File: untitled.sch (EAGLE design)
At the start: 31 parts, among them IC1 STM8S003F3

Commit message: second commit
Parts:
- added TP15: TPB2,54, testpad:TPB2,54
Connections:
- removed net N$25: C1.2, C5.2, IC1.GND, SWIM.3
- new net N$1: IC1.PC4/TIM1_CH4/CLK_CCO/AIN2/[!TIM1_CH2!], TP15.TP
- net GND: now also C1.2, C5.2, IC1.GND, SWIM.3
- net NEXT: now also IC1.PC7/SPI_MISO/[TIM1_CH2]; no longer IC1.PD4/UART1_CK/TIM2_CH1/BEEP
- net PLAY_PAUSE: now also IC1.PD3/AIN4/TIM2_CH2/ADC_ETR; no longer IC1.PD6/UART1_RX/AIN6
- net PRE: now also IC1.PD2/AIN3/[TIM2_CH3]; no longer IC1.PD5/UART1_TX/AIN5
- net VOL+: now also IC1.PC5/SPI_SCK/[TIM2_CH1]; no longer IC1.PD2/AIN3/[TIM2_CH3]
- net VOL-: now also IC1.PC6/SPI_MOSI/[TIM1_CH1]; no longer IC1.PD3/AIN4/TIM2_CH2/ADC_ETR

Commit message: third commit
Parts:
- removed TP1, TP2: TPB2,54, testpad:TPB2,54
- added SWIM1: (no value), con-lstb:MA04-1
- added U$2: MCP1825SOT-223-3, SteelCaveRobotics-Power:MCP1825SOT-223-3
- LED1, LED2, LED3: device led:LEDCHIP-LED0805 -> led:LEDCHIPLED_0603
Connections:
- removed net N$13: TP1.TP, U$1.UART_TX/PIO1
- removed net N$14: TP2.TP, U$1.UART_RX/PIO0
- new net VDD: TP13.TP, U$2.IN
- net GND: now also U$2.GND@2
- net LED0: now also LED3.C; no longer LED1.C
- net LED2: now also LED1.C; no longer LED3.C
- net N$1: now also IC1.PD6/UART1_RX/AIN6; no longer IC1.PC4/TIM1_CH4/CLK_CCO/AIN2/[!TIM1_CH2!]
- net N$20: now also SWIM1.1
- net N$21: now also SWIM1.2
- net N$22: now also SWIM1.3
- net N$23: now also SWIM1.4
- net N$4: now also LED1.A; no longer LED3.A
- net N$6: now also LED3.A; no longer LED1.A
- net VCC: now also U$2.+3V3; no longer TP13.TP
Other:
- moved on the sheet: LED1, LED3, TP13, TP15

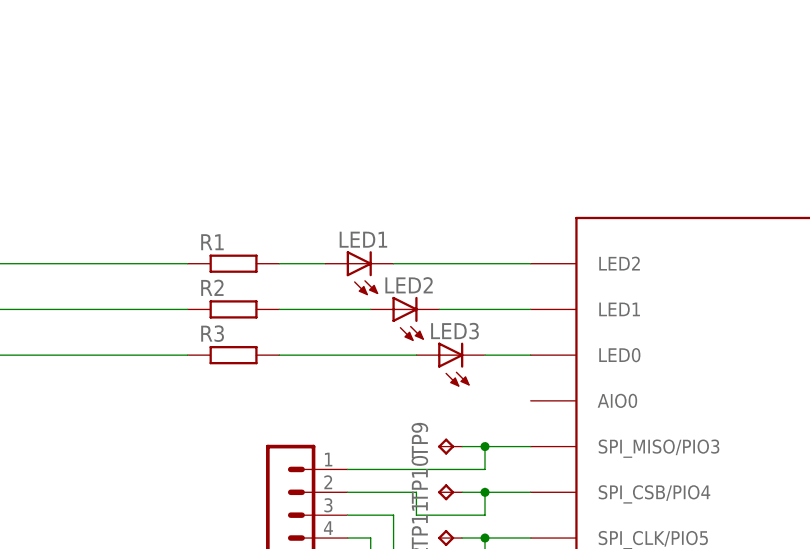
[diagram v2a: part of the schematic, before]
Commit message: removed leds
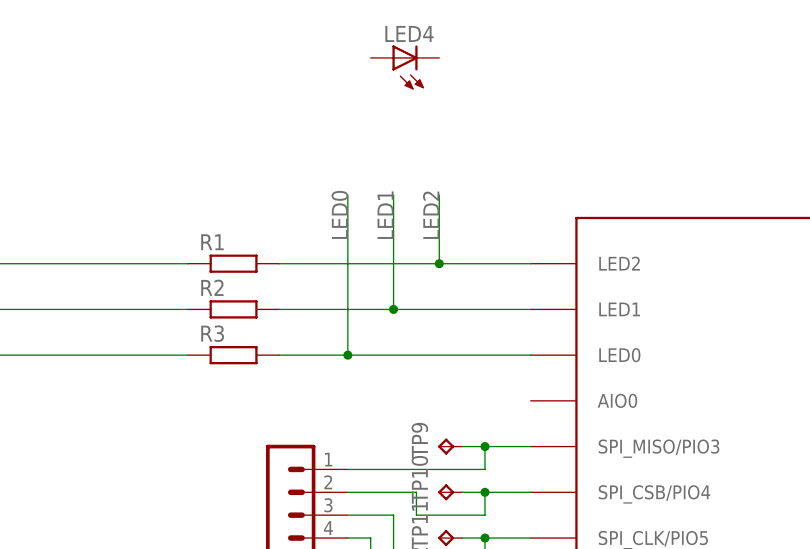
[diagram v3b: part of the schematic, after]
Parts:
- removed LED1, LED2, LED3: (no value), led:LEDCHIPLED_0603
- added LED4: (no value), led:LEDCHIPLED_0603
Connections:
- removed net N$4: LED1.A, R1.2
- removed net N$5: LED2.A, R2.2
- removed net N$6: LED3.A, R3.2
- net LED0: now also R3.2; no longer LED3.C
- net LED1: now also R2.2; no longer LED2.C
- net LED2: now also R1.2; no longer LED1.C
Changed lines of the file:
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@@
 <?xml version="1.0" encoding="utf-8"?>
 <!DOCTYPE eagle SYSTEM "eagle.dtd">
-<eagle version="7.3.0">
+<eagle version="7.4.0">
 <drawing>
 <settings>
@@
 <part name="TP15" library="testpad" deviceset="TP" device="B2,54"/>
 <part name="SWIM1" library="con-lstb" deviceset="MA04-1" device=""/>
-<part name="LED1" library="led" deviceset="LED" device="CHIPLED_0603"/>
-<part name="LED2" library="led" deviceset="LED" device="CHIPLED_0603"/>
-<part name="LED3" library="led" deviceset="LED" device="CHIPLED_0603"/>
 <part name="P+5" library="supply1" deviceset="VCC" device=""/>
 <part name="VDD1" library="supply1" deviceset="VDD" device=""/>
 <part name="U$2" library="SteelCaveRobotics-Power" deviceset="MCP1825" device="SOT-223-3"/>
 <part name="GND5" library="supply1" deviceset="GND" device=""/>
+<part name="LED4" library="led" deviceset="LED" device="CHIPLED_0603"/>
 </parts>
 <sheets>
@@
 <instance part="TP15" gate="G$1" x="238.76" y="-5.08" rot="R270"/>
 <instance part="SWIM1" gate="1" x="-63.5" y="12.7" rot="MR180"/>
-<instance part="LED1" gate="G$1" x="-55.88" y="40.64" rot="R90"/>
-<instance part="LED2" gate="G$1" x="-50.8" y="35.56" rot="R90"/>
-<instance part="LED3" gate="G$1" x="-45.72" y="30.48" rot="R90"/>
 <instance part="P+5" gate="VCC" x="-91.44" y="-33.02" rot="R270"/>
 <instance part="VDD1" gate="G$1" x="-127" y="-33.02" rot="R90"/>
 <instance part="U$2" gate="G$1" x="-109.22" y="-35.56"/>
 <instance part="GND5" gate="1" x="-109.22" y="-50.8"/>
+<instance part="LED4" gate="G$1" x="-50.8" y="63.5" rot="R90"/>
 </instances>
 <busses>
 </busses>
 <nets>
-<net name="N$4" class="0">
-<segment>
-<pinref part="R1" gate="G$1" pin="2"/>
-<wire x1="-58.42" y1="40.64" x2="-63.5" y2="40.64" width="0.1524" layer="91"/>
-<pinref part="LED1" gate="G$1" pin="A"/>
-</segment>
-</net>
-<net name="N$5" class="0">
-<segment>
-<pinref part="R2" gate="G$1" pin="2"/>
-<wire x1="-53.34" y1="35.56" x2="-63.5" y2="35.56" width="0.1524" layer="91"/>
-<pinref part="LED2" gate="G$1" pin="A"/>
-</segment>
-</net>
-<net name="N$6" class="0">
-<segment>
-<pinref part="R3" gate="G$1" pin="2"/>
-<wire x1="-48.26" y1="30.48" x2="-63.5" y2="30.48" width="0.1524" layer="91"/>
-<pinref part="LED3" gate="G$1" pin="A"/>
-</segment>
-</net>
 <net name="VCC" class="0">
 <segment>
@@
 <segment>
 <pinref part="U$1" gate="G$1" pin="LED2"/>
-<wire x1="-35.56" y1="40.64" x2="-50.8" y2="40.64" width="0.1524" layer="91"/>
-<pinref part="LED1" gate="G$1" pin="C"/>
+<wire x1="-35.56" y1="40.64" x2="-45.72" y2="40.64" width="0.1524" layer="91"/>
+<pinref part="R1" gate="G$1" pin="2"/>
+<wire x1="-45.72" y1="40.64" x2="-63.5" y2="40.64" width="0.1524" layer="91"/>
+<wire x1="-45.72" y1="40.64" x2="-45.72" y2="48.26" width="0.1524" layer="91"/>
+<junction x="-45.72" y="40.64"/>
+<label x="-45.72" y="43.18" size="1.778" layer="95" rot="R90"/>
 </segment>
 </net>
@@
 <segment>
 <pinref part="U$1" gate="G$1" pin="LED1"/>
-<wire x1="-35.56" y1="35.56" x2="-45.72" y2="35.56" width="0.1524" layer="91"/>
-<pinref part="LED2" gate="G$1" pin="C"/>
+<wire x1="-35.56" y1="35.56" x2="-50.8" y2="35.56" width="0.1524" layer="91"/>
+<pinref part="R2" gate="G$1" pin="2"/>
+<wire x1="-50.8" y1="35.56" x2="-63.5" y2="35.56" width="0.1524" layer="91"/>
+<wire x1="-50.8" y1="35.56" x2="-50.8" y2="48.26" width="0.1524" layer="91"/>
+<junction x="-50.8" y="35.56"/>
+<label x="-50.8" y="43.18" size="1.778" layer="95" rot="R90"/>
 </segment>
 </net>
@@
 <segment>
 <pinref part="U$1" gate="G$1" pin="LED0"/>
-<wire x1="-35.56" y1="30.48" x2="-40.64" y2="30.48" width="0.1524" layer="91"/>
-<pinref part="LED3" gate="G$1" pin="C"/>
-</segment>
-</net>
+<pinref part="R3" gate="G$1" pin="2"/>
+<wire x1="-35.56" y1="30.48" x2="-55.88" y2="30.48" width="0.1524" layer="91"/>
+<wire x1="-55.88" y1="30.48" x2="-63.5" y2="30.48" width="0.1524" layer="91"/>
+<wire x1="-55.88" y1="30.48" x2="-55.88" y2="48.26" width="0.1524" layer="91"/>
+<junction x="-55.88" y="30.48"/>
+<label x="-55.88" y="43.18" size="1.778" layer="95" rot="R90"/>
+</segment>
+</net>

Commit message: added tx signal + led
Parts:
- added R6: 100, rcl:R-EU_R0805
- added TP1: TPB2,54, testpad:TPB2,54
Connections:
- new net N$29: LED4.C, R6.1
- new net N$5: IC1.PD5/UART1_TX/AIN5, TP1.TP
- new net N$6: IC1.PB5/I2C_SDA/[TIM1_BKIN], LED4.A
- net GND: now also R6.2
- net LED0: now also IC1.PA3/TIM2_CH3/[SPI_NSS]; no longer IC1.PB5/I2C_SDA/[TIM1_BKIN]
- net LED1: no longer IC1.PB4/I2C_SCL/[ADC_ETR]
- net LED2: no longer IC1.PA3/TIM2_CH3/[SPI_NSS]
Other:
- moved on the sheet: LED4
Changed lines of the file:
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@@
 <?xml version="1.0" encoding="utf-8"?>
 <!DOCTYPE eagle SYSTEM "eagle.dtd">
-<eagle version="7.4.0">
+<eagle version="7.3.0">
 <drawing>
 <settings>
@@
 <part name="GND5" library="supply1" deviceset="GND" device=""/>
 <part name="LED4" library="led" deviceset="LED" device="CHIPLED_0603"/>
+<part name="TP1" library="testpad" deviceset="TP" device="B2,54"/>
+<part name="R6" library="rcl" deviceset="R-EU_" device="R0805" value="100"/>
+<part name="GND4" library="supply1" deviceset="GND" device=""/>
 </parts>
 <sheets>
@@
 <instance part="U$2" gate="G$1" x="-109.22" y="-35.56"/>
 <instance part="GND5" gate="1" x="-109.22" y="-50.8"/>
-<instance part="LED4" gate="G$1" x="-50.8" y="63.5" rot="R90"/>
+<instance part="LED4" gate="G$1" x="236.22" y="27.94" rot="R90"/>
+<instance part="TP1" gate="G$1" x="238.76" y="-2.54" rot="R270"/>
+<instance part="R6" gate="G$1" x="248.92" y="27.94"/>
+<instance part="GND4" gate="1" x="259.08" y="27.94" rot="R90"/>
 </instances>
 <busses>
@@
 <wire x1="-109.22" y1="-43.18" x2="-109.22" y2="-48.26" width="0.1524" layer="91"/>
 </segment>
+<segment>
+<pinref part="R6" gate="G$1" pin="2"/>
+<pinref part="GND4" gate="1" pin="GND"/>
+<wire x1="254" y1="27.94" x2="256.54" y2="27.94" width="0.1524" layer="91"/>
+</segment>
 </net>
 <net name="N$9" class="0">
@@
 <net name="LED2" class="0">
 <segment>
-<pinref part="IC1" gate="G$1" pin="PA3/TIM2_CH3/[SPI_NSS]"/>
-<wire x1="223.52" y1="33.02" x2="238.76" y2="33.02" width="0.1524" layer="91"/>
-<label x="233.68" y="33.02" size="1.778" layer="95"/>
-</segment>
-<segment>
 <pinref part="U$1" gate="G$1" pin="LED2"/>
 <wire x1="-35.56" y1="40.64" x2="-45.72" y2="40.64" width="0.1524" layer="91"/>
@@
 <net name="LED1" class="0">
 <segment>
-<pinref part="IC1" gate="G$1" pin="PB4/I2C_SCL/[ADC_ETR]"/>
-<wire x1="223.52" y1="30.48" x2="238.76" y2="30.48" width="0.1524" layer="91"/>
-<label x="233.68" y="30.48" size="1.778" layer="95"/>
-</segment>
-<segment>
 <pinref part="U$1" gate="G$1" pin="LED1"/>
 <wire x1="-35.56" y1="35.56" x2="-50.8" y2="35.56" width="0.1524" layer="91"/>
@@
 <net name="LED0" class="0">
 <segment>
-<pinref part="IC1" gate="G$1" pin="PB5/I2C_SDA/[TIM1_BKIN]"/>
-<wire x1="223.52" y1="27.94" x2="238.76" y2="27.94" width="0.1524" layer="91"/>
-<label x="233.68" y="27.94" size="1.778" layer="95"/>
-</segment>
-<segment>
 <pinref part="U$1" gate="G$1" pin="LED0"/>
 <pinref part="R3" gate="G$1" pin="2"/>
@@
 <label x="-55.88" y="43.18" size="1.778" layer="95" rot="R90"/>
 </segment>
+<segment>
+<pinref part="IC1" gate="G$1" pin="PA3/TIM2_CH3/[SPI_NSS]"/>
+<wire x1="223.52" y1="33.02" x2="238.76" y2="33.02" width="0.1524" layer="91"/>
+<label x="233.68" y="33.02" size="1.778" layer="95"/>
+</segment>
 </net>
 <net name="N$1" class="0">
@@
 </segment>
 </net>
+<net name="N$5" class="0">
+<segment>
+<pinref part="IC1" gate="G$1" pin="PD5/UART1_TX/AIN5"/>
+<pinref part="TP1" gate="G$1" pin="TP"/>
+<wire x1="223.52" y1="-2.54" x2="236.22" y2="-2.54" width="0.1524" layer="91"/>
+</segment>
+</net>
+<net name="N$6" class="0">
+<segment>
+<pinref part="IC1" gate="G$1" pin="PB5/I2C_SDA/[TIM1_BKIN]"/>
+<pinref part="LED4" gate="G$1" pin="A"/>
+<wire x1="223.52" y1="27.94" x2="233.68" y2="27.94" width="0.1524" layer="91"/>
+</segment>
+</net>
+<net name="N$29" class="0">
+<segment>
+<pinref part="LED4" gate="G$1" pin="C"/>
+<pinref part="R6" gate="G$1" pin="1"/>
+<wire x1="241.3" y1="27.94" x2="243.84" y2="27.94" width="0.1524" layer="91"/>
+</segment>
+</net>

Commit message: new design
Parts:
- removed TP10, TP11, TP12, TP9: TPB2,54, testpad:TPB2,54
- added C6, C7: 104, rcl:C-EUC0805
- added LED1: (no value), led:LEDCHIPLED_0603
- added R10, R7, R8, R9: (no value), rcl:R-EU_R0805
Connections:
- new net N$30: R8.2, U$1.SPI_CSB/PIO4
- new net N$31: R9.1, SWIM1.3
- new net N$32: R10.2, U$1.SPI_MOSI/PIO2
- new net N$33: R10.1, SWIM1.4
- new net N$34: LED1.C, U$1.LED1
- net GND: now also C6.2, C7.2
- net LED1: now also LED1.A; no longer U$1.LED1
- net N$20: now also R7.2; no longer SWIM1.1, TP9.TP
- net N$21: now also R7.1, SWIM1.1; no longer SWIM1.2, TP10.TP, U$1.SPI_CSB/PIO4
- net N$22: now also R9.2; no longer SWIM1.3, TP11.TP
- net N$23: now also R8.1, SWIM1.2; no longer SWIM1.4, TP12.TP, U$1.SPI_MOSI/PIO2
- net VCC: now also C7.1
- net VDD: now also C6.1
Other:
- moved on the sheet: SWIM1
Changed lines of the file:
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@@
 <part name="TP7" library="testpad" deviceset="TP" device="B2,54"/>
 <part name="TP8" library="testpad" deviceset="TP" device="B2,54"/>
-<part name="TP9" library="testpad" deviceset="TP" device="B2,54"/>
-<part name="TP10" library="testpad" deviceset="TP" device="B2,54"/>
-<part name="TP11" library="testpad" deviceset="TP" device="B2,54"/>
-<part name="TP12" library="testpad" deviceset="TP" device="B2,54"/>
 <part name="TP13" library="testpad" deviceset="TP" device="B2,54"/>
 <part name="TP14" library="testpad" deviceset="TP" device="B2,54"/>
@@
 <part name="R6" library="rcl" deviceset="R-EU_" device="R0805" value="100"/>
 <part name="GND4" library="supply1" deviceset="GND" device=""/>
+<part name="R7" library="rcl" deviceset="R-EU_" device="R0805"/>
+<part name="R8" library="rcl" deviceset="R-EU_" device="R0805"/>
+<part name="R9" library="rcl" deviceset="R-EU_" device="R0805"/>
+<part name="R10" library="rcl" deviceset="R-EU_" device="R0805"/>
+<part name="C6" library="rcl" deviceset="C-EU" device="C0805" value="104"/>
+<part name="C7" library="rcl" deviceset="C-EU" device="C0805" value="104"/>
+<part name="LED1" library="led" deviceset="LED" device="CHIPLED_0603"/>
 </parts>
 <sheets>
@@
 <instance part="TP7" gate="G$1" x="45.72" y="25.4" rot="R270"/>
 <instance part="TP8" gate="G$1" x="45.72" y="20.32" rot="R270"/>
-<instance part="TP9" gate="G$1" x="-45.72" y="20.32" rot="R90"/>
-<instance part="TP10" gate="G$1" x="-45.72" y="15.24" rot="R90"/>
-<instance part="TP11" gate="G$1" x="-45.72" y="10.16" rot="R90"/>
-<instance part="TP12" gate="G$1" x="-45.72" y="5.08" rot="R90"/>
 <instance part="TP13" gate="G$1" x="-121.92" y="-25.4"/>
 <instance part="TP14" gate="G$1" x="-53.34" y="-40.64" rot="R90"/>
@@
 <instance part="GND3" gate="1" x="129.54" y="5.08"/>
 <instance part="TP15" gate="G$1" x="238.76" y="-5.08" rot="R270"/>
-<instance part="SWIM1" gate="1" x="-63.5" y="12.7" rot="MR180"/>
+<instance part="SWIM1" gate="1" x="-66.04" y="12.7" rot="MR180"/>
 <instance part="P+5" gate="VCC" x="-91.44" y="-33.02" rot="R270"/>
 <instance part="VDD1" gate="G$1" x="-127" y="-33.02" rot="R90"/>
 <instance part="U$2" gate="G$1" x="-109.22" y="-35.56"/>
-<instance part="GND5" gate="1" x="-109.22" y="-50.8"/>
+<instance part="GND5" gate="1" x="-109.22" y="-55.88"/>
 <instance part="LED4" gate="G$1" x="236.22" y="27.94" rot="R90"/>
 <instance part="TP1" gate="G$1" x="238.76" y="-2.54" rot="R270"/>
 <instance part="R6" gate="G$1" x="248.92" y="27.94"/>
 <instance part="GND4" gate="1" x="259.08" y="27.94" rot="R90"/>
+<instance part="R7" gate="G$1" x="-45.72" y="20.32"/>
+<instance part="R8" gate="G$1" x="-45.72" y="15.24"/>
+<instance part="R9" gate="G$1" x="-45.72" y="10.16"/>
+<instance part="R10" gate="G$1" x="-45.72" y="5.08"/>
+<instance part="C6" gate="G$1" x="-121.92" y="-40.64"/>
+<instance part="C7" gate="G$1" x="-96.52" y="-40.64"/>
+<instance part="LED1" gate="G$1" x="-45.72" y="35.56" rot="R90"/>
 </instances>
 <busses>
@@
 <pinref part="U$2" gate="G$1" pin="+3V3"/>
 <pinref part="P+5" gate="VCC" pin="VCC"/>
-<wire x1="-99.06" y1="-33.02" x2="-93.98" y2="-33.02" width="0.1524" layer="91"/>
+<wire x1="-99.06" y1="-33.02" x2="-96.52" y2="-33.02" width="0.1524" layer="91"/>
+<pinref part="C7" gate="G$1" pin="1"/>
+<wire x1="-96.52" y1="-33.02" x2="-93.98" y2="-33.02" width="0.1524" layer="91"/>
+<wire x1="-96.52" y1="-38.1" x2="-96.52" y2="-33.02" width="0.1524" layer="91"/>
+<junction x="-96.52" y="-33.02"/>
 </segment>
 </net>
@@
 <pinref part="GND5" gate="1" pin="GND"/>
 <wire x1="-109.22" y1="-43.18" x2="-109.22" y2="-48.26" width="0.1524" layer="91"/>
+<pinref part="C6" gate="G$1" pin="2"/>
+<wire x1="-109.22" y1="-48.26" x2="-109.22" y2="-53.34" width="0.1524" layer="91"/>
+<wire x1="-121.92" y1="-45.72" x2="-121.92" y2="-48.26" width="0.1524" layer="91"/>
+<wire x1="-121.92" y1="-48.26" x2="-109.22" y2="-48.26" width="0.1524" layer="91"/>
+<junction x="-109.22" y="-48.26"/>
+<pinref part="C7" gate="G$1" pin="2"/>
+<wire x1="-96.52" y1="-45.72" x2="-96.52" y2="-48.26" width="0.1524" layer="91"/>
+<wire x1="-96.52" y1="-48.26" x2="-109.22" y2="-48.26" width="0.1524" layer="91"/>
 </segment>
 <segment>
@@
 <segment>
 <pinref part="U$1" gate="G$1" pin="SPI_MISO/PIO3"/>
-<pinref part="TP9" gate="G$1" pin="TP"/>
 <wire x1="-35.56" y1="20.32" x2="-40.64" y2="20.32" width="0.1524" layer="91"/>
-<pinref part="SWIM1" gate="1" pin="1"/>
-<wire x1="-40.64" y1="20.32" x2="-43.18" y2="20.32" width="0.1524" layer="91"/>
-<wire x1="-55.88" y1="17.78" x2="-40.64" y2="17.78" width="0.1524" layer="91"/>
-<wire x1="-40.64" y1="17.78" x2="-40.64" y2="20.32" width="0.1524" layer="91"/>
-<junction x="-40.64" y="20.32"/>
-</segment>
-</net>
-<net name="N$21" class="0">
-<segment>
-<pinref part="U$1" gate="G$1" pin="SPI_CSB/PIO4"/>
-<pinref part="TP10" gate="G$1" pin="TP"/>
-<wire x1="-35.56" y1="15.24" x2="-40.64" y2="15.24" width="0.1524" layer="91"/>
-<pinref part="SWIM1" gate="1" pin="2"/>
-<wire x1="-40.64" y1="15.24" x2="-43.18" y2="15.24" width="0.1524" layer="91"/>
-<wire x1="-55.88" y1="15.24" x2="-48.26" y2="15.24" width="0.1524" layer="91"/>
-<wire x1="-48.26" y1="15.24" x2="-48.26" y2="12.7" width="0.1524" layer="91"/>
-<wire x1="-48.26" y1="12.7" x2="-40.64" y2="12.7" width="0.1524" layer="91"/>
-<wire x1="-40.64" y1="12.7" x2="-40.64" y2="15.24" width="0.1524" layer="91"/>
-<junction x="-40.64" y="15.24"/>
+<pinref part="R7" gate="G$1" pin="2"/>
 </segment>
 </net>
@@
 <segment>
 <pinref part="U$1" gate="G$1" pin="SPI_CLK/PIO5"/>
-<pinref part="TP11" gate="G$1" pin="TP"/>
 <wire x1="-35.56" y1="10.16" x2="-40.64" y2="10.16" width="0.1524" layer="91"/>
-<pinref part="SWIM1" gate="1" pin="3"/>
-<wire x1="-40.64" y1="10.16" x2="-43.18" y2="10.16" width="0.1524" layer="91"/>
-<wire x1="-55.88" y1="12.7" x2="-50.8" y2="12.7" width="0.1524" layer="91"/>
-<wire x1="-50.8" y1="12.7" x2="-50.8" y2="7.62" width="0.1524" layer="91"/>
-<wire x1="-50.8" y1="7.62" x2="-40.64" y2="7.62" width="0.1524" layer="91"/>
-<wire x1="-40.64" y1="7.62" x2="-40.64" y2="10.16" width="0.1524" layer="91"/>
-<junction x="-40.64" y="10.16"/>
-</segment>
-</net>
-<net name="N$23" class="0">
-<segment>
-<pinref part="U$1" gate="G$1" pin="SPI_MOSI/PIO2"/>
-<pinref part="TP12" gate="G$1" pin="TP"/>
-<wire x1="-35.56" y1="5.08" x2="-40.64" y2="5.08" width="0.1524" layer="91"/>
-<pinref part="SWIM1" gate="1" pin="4"/>
-<wire x1="-40.64" y1="5.08" x2="-43.18" y2="5.08" width="0.1524" layer="91"/>
-<wire x1="-55.88" y1="10.16" x2="-53.34" y2="10.16" width="0.1524" layer="91"/>
-<wire x1="-53.34" y1="10.16" x2="-53.34" y2="2.54" width="0.1524" layer="91"/>
-<wire x1="-53.34" y1="2.54" x2="-40.64" y2="2.54" width="0.1524" layer="91"/>
-<wire x1="-40.64" y1="2.54" x2="-40.64" y2="5.08" width="0.1524" layer="91"/>
-<junction x="-40.64" y="5.08"/>
+<pinref part="R9" gate="G$1" pin="2"/>
 </segment>
 </net>
@@
 <net name="LED1" class="0">
 <segment>
-<pinref part="U$1" gate="G$1" pin="LED1"/>
-<wire x1="-35.56" y1="35.56" x2="-50.8" y2="35.56" width="0.1524" layer="91"/>
 <pinref part="R2" gate="G$1" pin="2"/>
 <wire x1="-50.8" y1="35.56" x2="-63.5" y2="35.56" width="0.1524" layer="91"/>
 <wire x1="-50.8" y1="35.56" x2="-50.8" y2="48.26" width="0.1524" layer="91"/>
+<label x="-50.8" y="43.18" size="1.778" layer="95" rot="R90"/>
+<pinref part="LED1" gate="G$1" pin="A"/>
+<wire x1="-48.26" y1="35.56" x2="-50.8" y2="35.56" width="0.1524" layer="91"/>
 <junction x="-50.8" y="35.56"/>
-<label x="-50.8" y="43.18" size="1.778" layer="95" rot="R90"/>
 </segment>
 </net>
@@
 <wire x1="-121.92" y1="-27.94" x2="-121.92" y2="-33.02" width="0.1524" layer="91"/>
 <junction x="-121.92" y="-33.02"/>
+<pinref part="C6" gate="G$1" pin="1"/>
+<wire x1="-121.92" y1="-38.1" x2="-121.92" y2="-33.02" width="0.1524" layer="91"/>
 </segment>
 </net>
@@
 </segment>
 </net>
+<net name="N$30" class="0">
+<segment>
+<pinref part="U$1" gate="G$1" pin="SPI_CSB/PIO4"/>
+<wire x1="-35.56" y1="15.24" x2="-40.64" y2="15.24" width="0.1524" layer="91"/>
+<pinref part="R8" gate="G$1" pin="2"/>
+</segment>
+</net>
+<net name="N$32" class="0">
+<segment>
+<pinref part="U$1" gate="G$1" pin="SPI_MOSI/PIO2"/>
+<wire x1="-35.56" y1="5.08" x2="-40.64" y2="5.08" width="0.1524" layer="91"/>
+<pinref part="R10" gate="G$1" pin="2"/>
+</segment>
+</net>
+<net name="N$21" class="0">
+<segment>
+<pinref part="SWIM1" gate="1" pin="1"/>
+<wire x1="-58.42" y1="17.78" x2="-53.34" y2="17.78" width="0.1524" layer="91"/>
+<wire x1="-53.34" y1="17.78" x2="-53.34" y2="20.32" width="0.1524" layer="91"/>
+<pinref part="R7" gate="G$1" pin="1"/>
+<wire x1="-53.34" y1="20.32" x2="-50.8" y2="20.32" width="0.1524" layer="91"/>
+</segment>
+</net>
+<net name="N$23" class="0">
+<segment>
+<pinref part="R8" gate="G$1" pin="1"/>
+<pinref part="SWIM1" gate="1" pin="2"/>
+<wire x1="-50.8" y1="15.24" x2="-58.42" y2="15.24" width="0.1524" layer="91"/>
+</segment>
+</net>
+<net name="N$31" class="0">
+<segment>
+<pinref part="SWIM1" gate="1" pin="3"/>
+<wire x1="-58.42" y1="12.7" x2="-53.34" y2="12.7" width="0.1524" layer="91"/>
+<wire x1="-53.34" y1="12.7" x2="-53.34" y2="10.16" width="0.1524" layer="91"/>
+<pinref part="R9" gate="G$1" pin="1"/>
+<wire x1="-53.34" y1="10.16" x2="-50.8" y2="10.16" width="0.1524" layer="91"/>
+</segment>
+</net>
+<net name="N$33" class="0">
+<segment>
+<pinref part="R10" gate="G$1" pin="1"/>
+<wire x1="-50.8" y1="5.08" x2="-55.88" y2="5.08" width="0.1524" layer="91"/>
+<wire x1="-55.88" y1="5.08" x2="-55.88" y2="10.16" width="0.1524" layer="91"/>
+<pinref part="SWIM1" gate="1" pin="4"/>
+<wire x1="-55.88" y1="10.16" x2="-58.42" y2="10.16" width="0.1524" layer="91"/>
+</segment>
+</net>
+<net name="N$34" class="0">
+<segment>
+<pinref part="LED1" gate="G$1" pin="C"/>
+<pinref part="U$1" gate="G$1" pin="LED1"/>
+<wire x1="-40.64" y1="35.56" x2="-35.56" y2="35.56" width="0.1524" layer="91"/>
+</segment>
+</net>
